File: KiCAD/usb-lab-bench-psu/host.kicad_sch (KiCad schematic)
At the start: 47 parts, among them J4 USB_C_Receptacle, SW1 SW_Push, SW2 SW_Push, U2 USBLC6-2SC6, U3 ESP32-C3, U4 ZD25WQ32C, U6 LMR16006X, Y1 40MHz

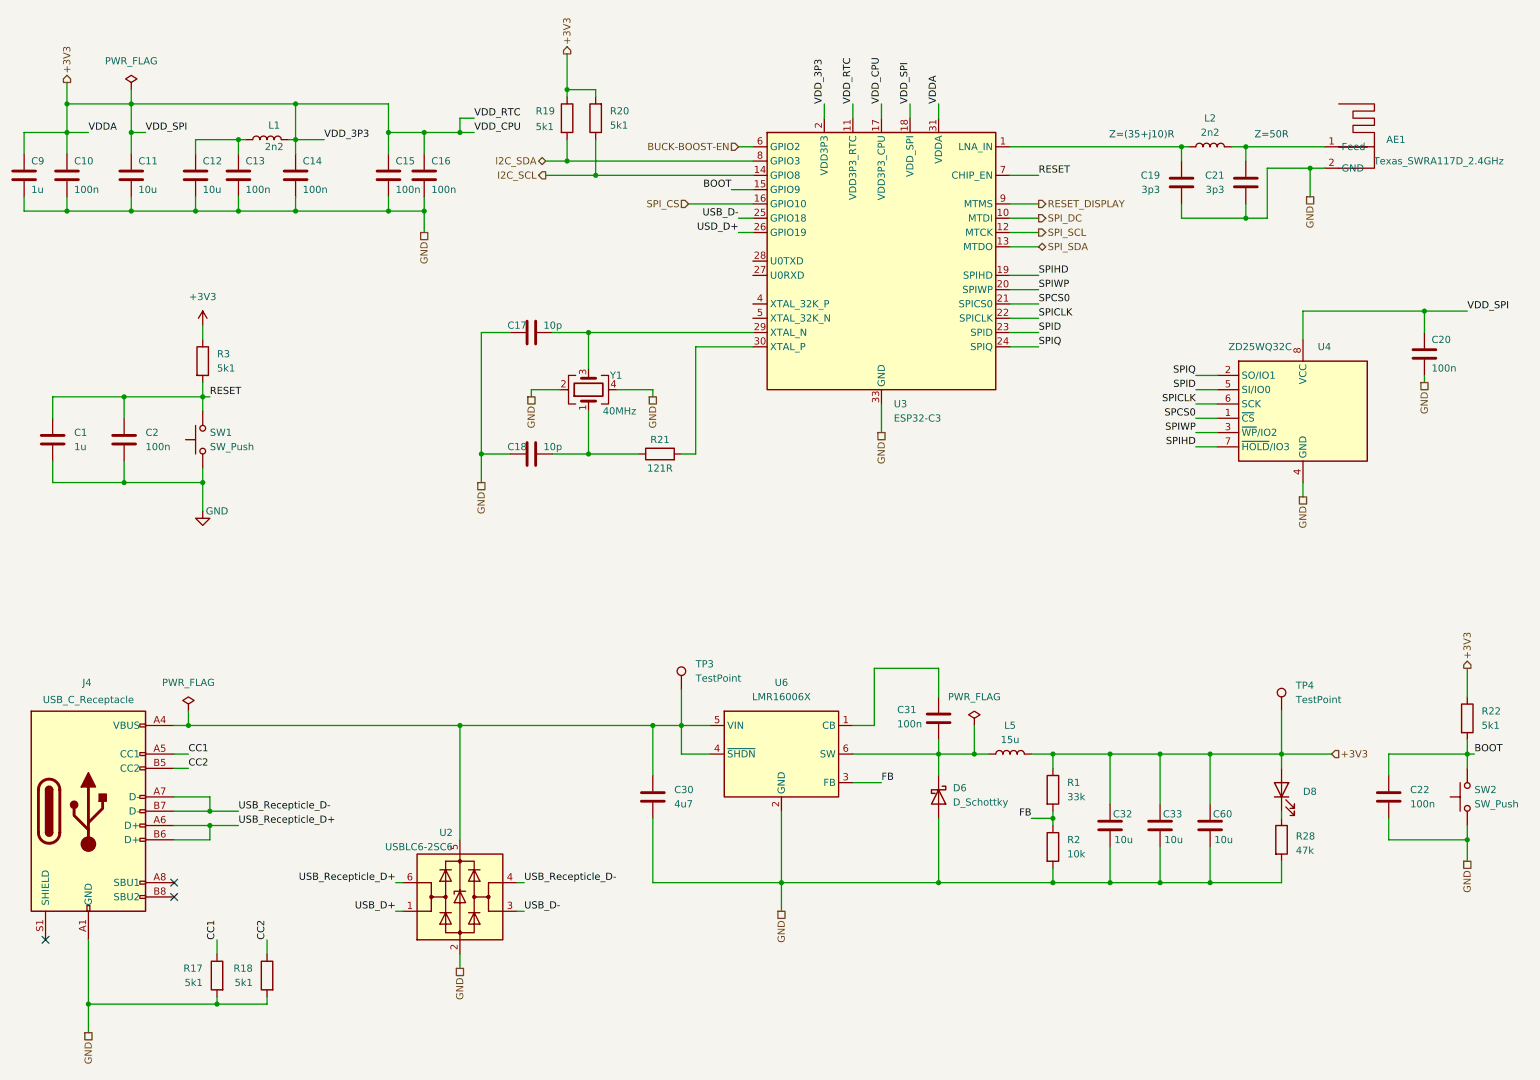
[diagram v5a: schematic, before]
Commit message: added current limiting circuit for USB PD sink, added 2nd buck converter
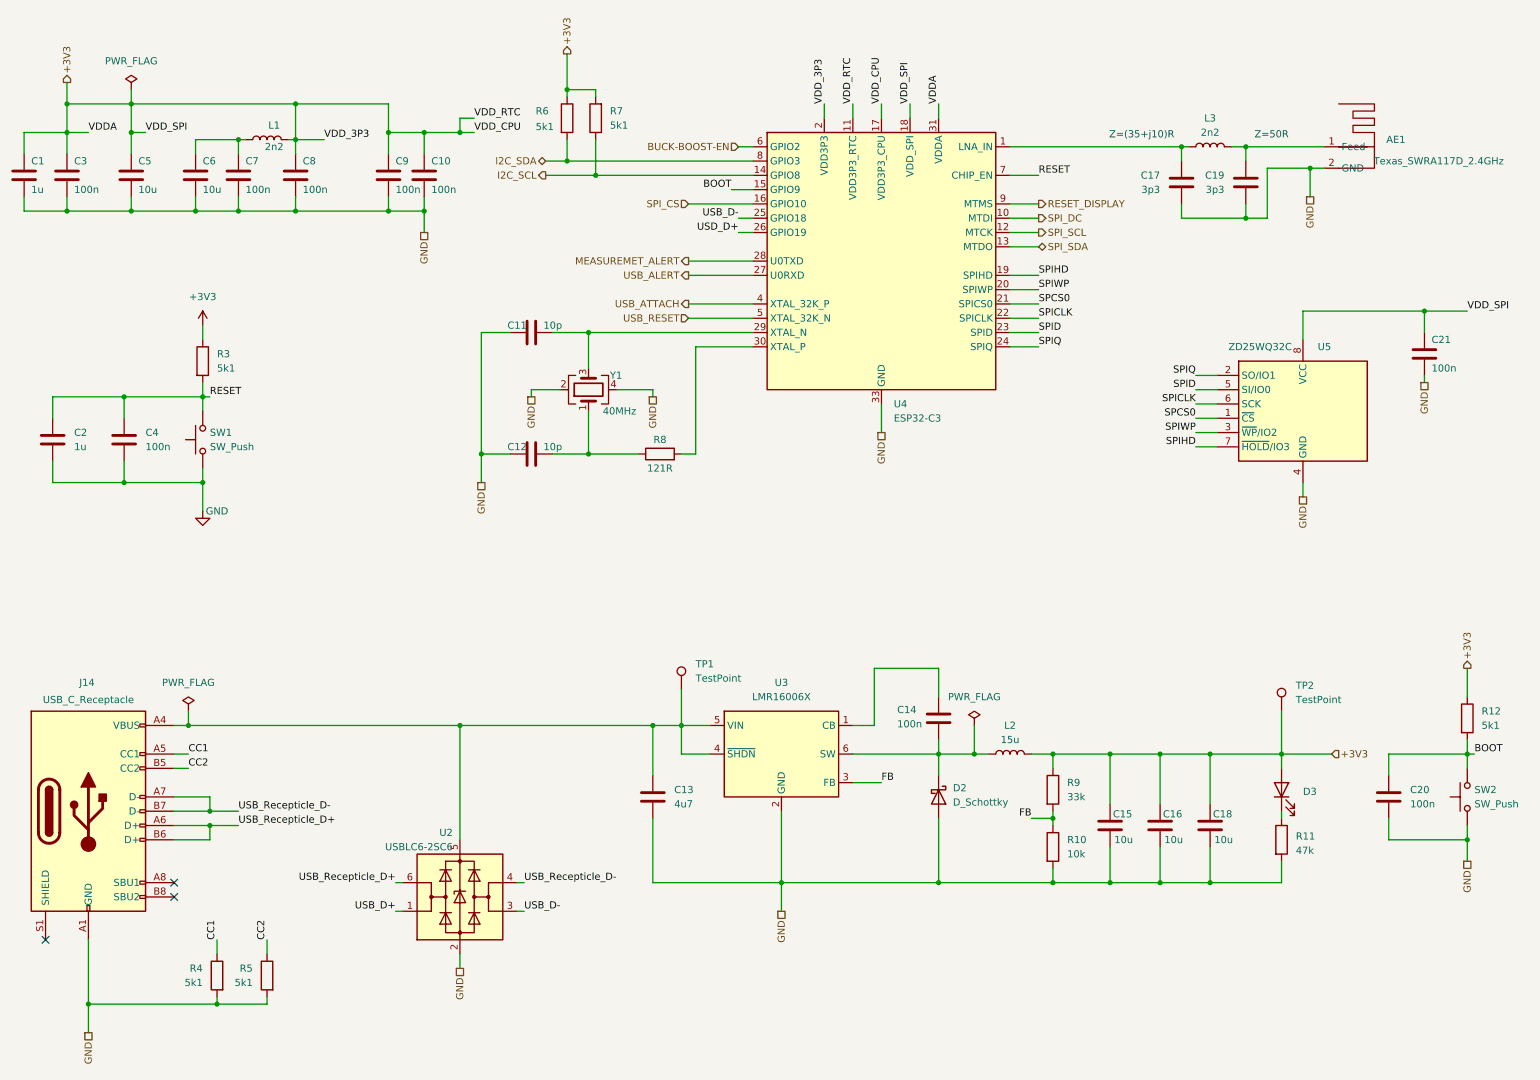
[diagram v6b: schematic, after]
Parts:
- renumbered C9 to C1, C16 to C10, C17 to C11, C18 to C12, C30 to C13, C31 to C14, C32 to C15, C33 to C16, C19 to C17, C60 to C18, C21 to C19, C1 to C2, C22 to C20, C20 to C21, C10 to C3, C2 to C4, C11 to C5, C12 to C6, C13 to C7, C14 to C8, C15 to C9, D6 to D2, D8 to D3, J4 to J14, L5 to L2, L2 to L3, R2 to R10, R28 to R11, R22 to R12, R17 to R4, R18 to R5, R19 to R6, R20 to R7, R21 to R8, R1 to R9, TP3 to TP1, TP4 to TP2, U6 to U3, U3 to U4, U4 to U5
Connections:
- net USB_ALERT: now reaches U4.27 (U0RXD)
- net MEASUREMET_ALERT: now reaches U4.28 (U0TXD)
- net USB_ATTACH: now reaches U4.4 (XTAL_32K_P)
- net USB_RESET: now reaches U4.5 (XTAL_32K_N)

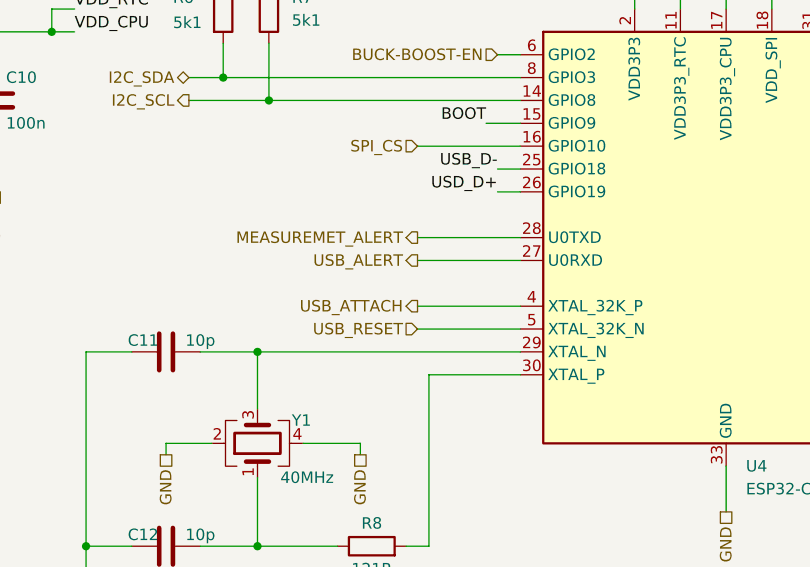
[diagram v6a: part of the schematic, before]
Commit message: tweaked design of current limiter, added GPIO expander to USB-PD circuit
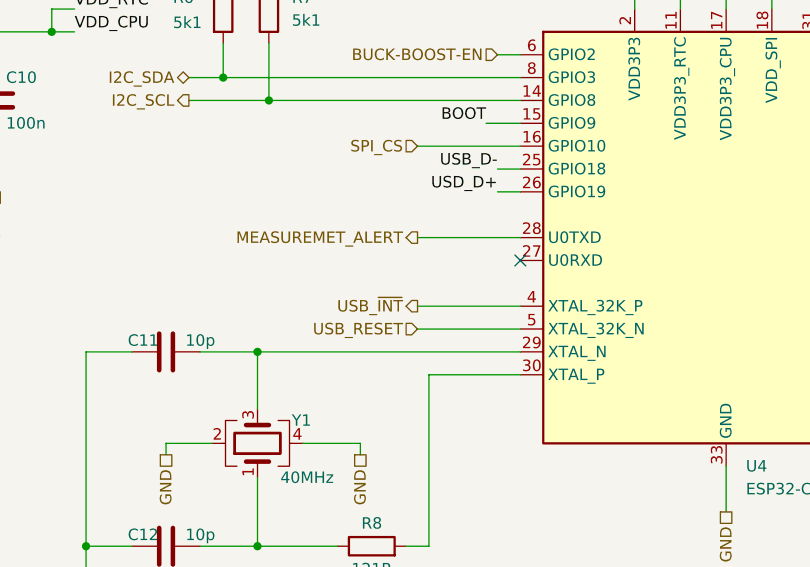
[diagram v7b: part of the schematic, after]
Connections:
- net USB_ALERT: no longer names the net of U4.27 (U0RXD)
- net USB_ATTACH renamed USB_~{INT}
- no-connect marks 3 -> 4
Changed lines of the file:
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@@
+	)
+	(no_connect
+		(at 146.05 55.88)
 	)
 	(no_connect
@@
 		(pts
 			(xy 87.63 34.29) (xy 87.63 30.48)
-		)
-		(stroke
-			(width 0)
-			(type default)
-		)
-	)
-	(wire
-		(pts
-			(xy 134.62 55.88) (xy 146.05 55.88)
 		)
 		(stroke
@@
 		)
 	)
-	(hierarchical_label "USB_ATTACH"
+	(hierarchical_label "USB_~{INT}"
 		(shape output)
 		(at 134.62 60.96 180)
 		(effects
 			(font
-				(size 1.27 1.27)
-			)
-			(justify right)
-		)
-	)
-	(hierarchical_label "USB_ALERT"
-		(shape output)
-		(at 134.62 55.88 180)
-		(effects
-			(font
